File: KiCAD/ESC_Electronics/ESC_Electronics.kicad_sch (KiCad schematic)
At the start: 57 parts, among them J1 -1000VDC, J2 Test Input, J3 CA probe, J4 DC Power, J5 Output, J6 Barrel_Jack, Q1 MMBT3906, Q2 MMBT3904, U1 CR110, U2 SiPhotodiode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

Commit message: laying out V1
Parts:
- added H1, H2, H3, H4: MountingHole, MountingHole:MountingHole_3.2mm_M3, symbol Mechanical:MountingHole
- added J7: -6V, Connector_PinHeader_2.54mm:PinHeader_1x02_P2.54mm_Vertical, symbol Connector_Generic:Conn_01x02
- added J8: +6V, Connector_PinHeader_2.54mm:PinHeader_1x02_P2.54mm_Vertical, symbol Connector_Generic:Conn_01x02
- added TH1: PTC 200mA, Fuse:Fuse_1210_3225Metric_Pad1.42x2.65mm_HandSolder, symbol Device:Thermistor_PTC_US
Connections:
- net +6VDC: now also J8.1 (Pin_1)
- net -6VDC: now also J7.1 (Pin_1)
- net GND: now also J7.2 (Pin_2), J8.2 (Pin_2)
- net at J6.1: now also TH1.2; no longer L1.1
- new net: L1.1, TH1.1
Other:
- moved on the sheet: J6

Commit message: layed out board
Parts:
- added H5: DiodeFeedThru, ESC_Electronics_Library:DiodeFeedThru, symbol Mechanical:MountingHole
- added R20: 10k, Resistor_THT:R_Axial_DIN0207_L6.3mm_D2.5mm_P5.08mm_Vertical, symbol Device:R_Small_US
- C6: value 1nF -> 1pF; Digikey 399-5094-ND -> 445-180733-1-ND
- R11: footprint Resistor_SMD:R_0805_2012Metric_Pad1.20x1.40mm_HandSolder -> Resistor_THT:R_Axial_DIN0207_L6.3mm_D2.5mm_P5.08mm_Vertical
- R12: value 20k -> 10k; footprint Resistor_SMD:R_0805_2012Metric_Pad1.20x1.40mm_HandSolder -> Resistor_THT:R_Axial_DIN0207_L6.3mm_D2.5mm_P5.08mm_Vertical
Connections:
- net GND: now also C9.2, R12.1, U3.4 (VCC-)
- net at J5.1 (In), U3.1 (1OUT): now also R20.2; no longer R12.1
- net at R11.2, U3.3 (1IN+): no longer R12.2
- new net: R12.2, R20.1, U3.2 (1IN-)
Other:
- note added: "A = 1+R20/R12"
- moved on the sheet: J5, R12

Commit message: uploaded this version to OSHpark as V1
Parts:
- added H6, H7: MountingHole, ESC_Electronics_Library:4headclear, symbol Mechanical:MountingHole
- C1, C4: footprint Capacitor_SMD:C_1206_3216Metric_Pad1.33x1.80mm_HandSolder -> Capacitor_SMD:C_0805_2012Metric_Pad1.18x1.45mm_HandSolder; Digikey 1276-6767-1-ND -> 1276-1096-1-ND
- C7: Digikey 445-181037-ND -> 445-175513-ND
- C9: Digikey (none) -> 1276-1099-1-ND
- D1, D2, D3, D4: Digikey (none) -> 3757-RB751V-40-AU_R1_000A1CT-ND
- J6: Digikey 2368-57-PJ70-ND -> 839-1580-ND
- R12: Digikey RNCP0805FTD20K0CT-ND -> (none)
- R18, R19: footprint Resistor_SMD:R_0805_2012Metric_Pad1.20x1.40mm_HandSolder -> Resistor_SMD:R_1206_3216Metric_Pad1.30x1.75mm_HandSolder; Digikey RNCP0805FTD20R0CT-ND -> RNCP1206FTD20R0CT-ND

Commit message: the real ESC V1
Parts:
- U2: footprint Connector_Wire:SolderWire-2sqmm_1x02_P7.8mm_D2mm_OD3.9mm -> Connector_Wire:SolderWire-1sqmm_1x02_P7.8mm_D1.4mm_OD3.9mm
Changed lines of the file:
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@@
     (property "Reference" "U2" (id 0) (at 64.77 66.04 0))
     (property "Value" "SiPhotodiode" (id 1) (at 64.77 80.01 0))
-    (property "Footprint" "Connector_Wire:SolderWire-2sqmm_1x02_P7.8mm_D2mm_OD3.9mm" (id 2) (at 64.77 74.93 0)
+    (property "Footprint" "Connector_Wire:SolderWire-1sqmm_1x02_P7.8mm_D1.4mm_OD3.9mm" (id 2) (at 64.77 74.93 0)
       (effects (font (size 1.27 1.27)) hide)
     )
@@
     )
     (path "/e6c36a61-be9b-4e0e-80a4-d48420033ad2"
-      (reference "U2") (unit 1) (value "SiPhotodiode") (footprint "Connector_Wire:SolderWire-2sqmm_1x02_P7.8mm_D2mm_OD3.9mm")
+      (reference "U2") (unit 1) (value "SiPhotodiode") (footprint "Connector_Wire:SolderWire-1sqmm_1x02_P7.8mm_D1.4mm_OD3.9mm")
     )
     (path "/97bce208-2f33-403f-8d9d-1ed134dba1dc"

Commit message: Refining for V2 while debugging
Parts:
- added C?: 0.1uF, Capacitor_SMD:C_0805_2012Metric_Pad1.18x1.45mm_HandSolder, symbol Device:C_Small
- D5, D6: value MM3Z6V8 -> MM3Z7V5T1G; Digikey MM3Z6V8T1GOSCT-ND -> MM3Z7V5T1GOSCT-ND
- R11, R12, R20: footprint Resistor_THT:R_Axial_DIN0207_L6.3mm_D2.5mm_P5.08mm_Vertical -> Resistor_THT:R_Axial_DIN0207_L6.3mm_D2.5mm_P10.16mm_Horizontal
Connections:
- net -6VDC: now also U3.4 (VCC-), C?.1
- net GND: now also D6.2 (A), C?.2; no longer D6.1 (K), U3.4 (VCC-)
- net at C12.1, Q2.1 (B), R16.2: now also D6.1 (K); no longer D6.2 (A)
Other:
- note added: "V1-V2 Changes: D6 orientation was backwards"
- note added: "V1: Initial Design (works w/ mods) V2: D6 orientation fixed, U3 VCC- power now -6V, change zeener D5/6 to 7.5V"
- moved on the sheet: C9, D6

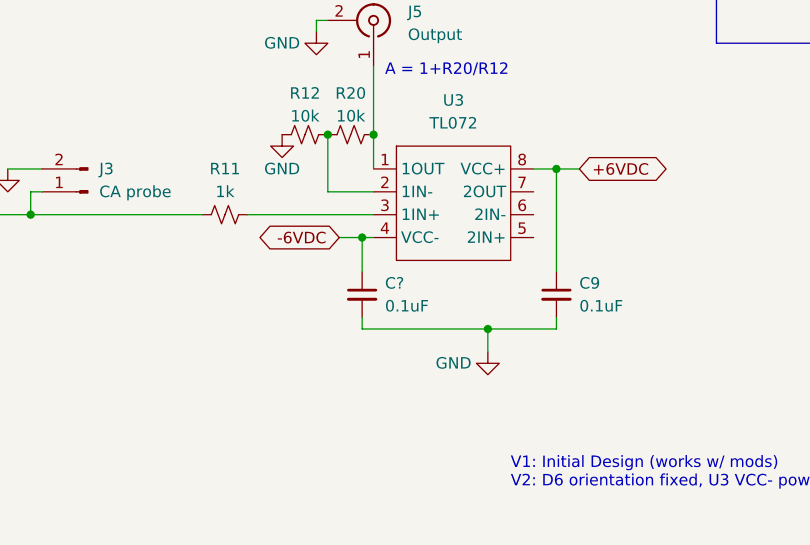
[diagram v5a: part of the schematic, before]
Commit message: Refining for V2 while debugging R2
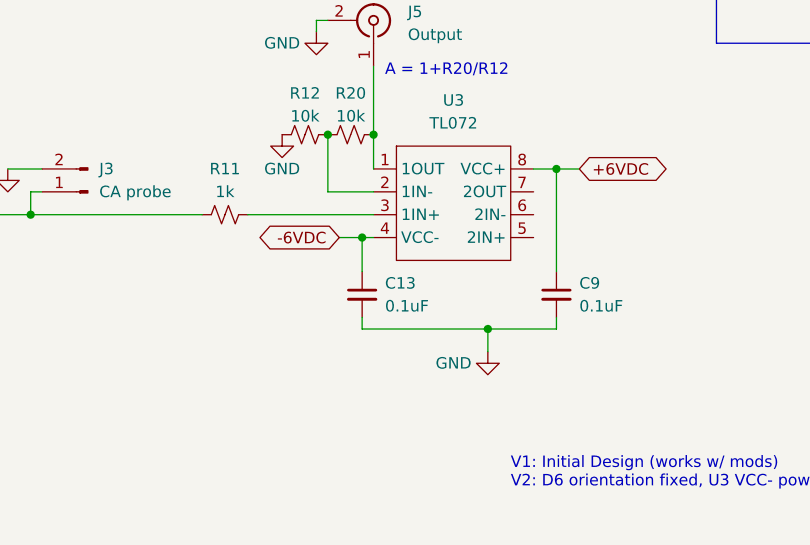
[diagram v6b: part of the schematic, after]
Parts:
- J6: footprint Connector_Wire:SolderWire-0.75sqmm_1x02_P7mm_D1.25mm_OD3.5mm -> Connector_Wire:SolderWire-0.5sqmm_1x02_P4.6mm_D0.9mm_OD2.1mm
- U2: footprint Connector_Wire:SolderWire-1sqmm_1x02_P7.8mm_D1.4mm_OD3.9mm -> Connector_Wire:SolderWire-0.5sqmm_1x02_P4.6mm_D0.9mm_OD2.1mm
- gave numbers to parts that had none: 1
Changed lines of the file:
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@@
   (symbol (lib_id "Device:C_Small") (at 161.29 148.59 0) (unit 1)
     (in_bom yes) (on_board yes) (fields_autoplaced)
-    (property "Reference" "C?" (id 0) (at 163.83 147.3262 0)
+    (property "Reference" "C13" (id 0) (at 163.83 147.3262 0)
       (effects (font (size 1.27 1.27)) (justify left))
     )
@@
     (property "Reference" "J6" (id 0) (at 144.78 59.69 0))
     (property "Value" "Barrel_Jack" (id 1) (at 144.78 62.23 0))
-    (property "Footprint" "Connector_Wire:SolderWire-0.75sqmm_1x02_P7mm_D1.25mm_OD3.5mm" (id 2) (at 146.05 69.596 0)
+    (property "Footprint" "Connector_Wire:SolderWire-0.5sqmm_1x02_P4.6mm_D0.9mm_OD2.1mm" (id 2) (at 146.05 69.596 0)
       (effects (font (size 1.27 1.27)) hide)
     )
@@
     (property "Reference" "U2" (id 0) (at 64.77 66.04 0))
     (property "Value" "SiPhotodiode" (id 1) (at 64.77 80.01 0))
-    (property "Footprint" "Connector_Wire:SolderWire-1sqmm_1x02_P7.8mm_D1.4mm_OD3.9mm" (id 2) (at 64.77 74.93 0)
+    (property "Footprint" "Connector_Wire:SolderWire-0.5sqmm_1x02_P4.6mm_D0.9mm_OD2.1mm" (id 2) (at 64.77 74.93 0)
       (effects (font (size 1.27 1.27)) hide)
     )
@@
     )
     (path "/15f60ce8-f9f6-4219-a4f7-60b75ad13587"
-      (reference "C?") (unit 1) (value "0.1uF") (footprint "Capacitor_SMD:C_0805_2012Metric_Pad1.18x1.45mm_HandSolder")
+      (reference "C13") (unit 1) (value "0.1uF") (footprint "Capacitor_SMD:C_0805_2012Metric_Pad1.18x1.45mm_HandSolder")
     )
     (path "/4279194e-067c-4776-b21d-089a47132a3b"
@@
     )
     (path "/35cfbf87-dcaf-4d5c-832e-d9611d138f98"
-      (reference "J6") (unit 1) (value "Barrel_Jack") (footprint "Connector_Wire:SolderWire-0.75sqmm_1x02_P7mm_D1.25mm_OD3.5mm")
+      (reference "J6") (unit 1) (value "Barrel_Jack") (footprint "Connector_Wire:SolderWire-0.5sqmm_1x02_P4.6mm_D0.9mm_OD2.1mm")
     )
     (path "/9130d071-ea24-455f-bfb6-ea618ccf9d3d"
@@
     )
     (path "/e6c36a61-be9b-4e0e-80a4-d48420033ad2"
-      (reference "U2") (unit 1) (value "SiPhotodiode") (footprint "Connector_Wire:SolderWire-1sqmm_1x02_P7.8mm_D1.4mm_OD3.9mm")
+      (reference "U2") (unit 1) (value "SiPhotodiode") (footprint "Connector_Wire:SolderWire-0.5sqmm_1x02_P4.6mm_D0.9mm_OD2.1mm")
     )
     (path "/97bce208-2f33-403f-8d9d-1ed134dba1dc"

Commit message: Refining for V2 while debugging R3
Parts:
- R3, R4, R5, R6, R8: footprint Resistor_THT:R_Axial_DIN0207_L6.3mm_D2.5mm_P7.62mm_Horizontal -> Resistor_THT:R_Axial_DIN0207_L6.3mm_D2.5mm_P10.16mm_Horizontal
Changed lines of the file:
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@@
       (effects (font (size 1.27 1.27)) (justify right))
     )
-    (property "Footprint" "Resistor_THT:R_Axial_DIN0207_L6.3mm_D2.5mm_P7.62mm_Horizontal" (id 2) (at 77.47 93.98 0)
+    (property "Footprint" "Resistor_THT:R_Axial_DIN0207_L6.3mm_D2.5mm_P10.16mm_Horizontal" (id 2) (at 77.47 93.98 0)
       (effects (font (size 1.27 1.27)) hide)
     )
@@
     (property "Reference" "R5" (id 0) (at 80.01 68.58 90))
     (property "Value" "100M" (id 1) (at 80.01 71.12 90))
-    (property "Footprint" "Resistor_THT:R_Axial_DIN0207_L6.3mm_D2.5mm_P7.62mm_Horizontal" (id 2) (at 80.01 74.93 0)
+    (property "Footprint" "Resistor_THT:R_Axial_DIN0207_L6.3mm_D2.5mm_P10.16mm_Horizontal" (id 2) (at 80.01 74.93 0)
       (effects (font (size 1.27 1.27)) hide)
     )
@@
       (effects (font (size 1.27 1.27)) (justify right))
     )
-    (property "Footprint" "Resistor_THT:R_Axial_DIN0207_L6.3mm_D2.5mm_P7.62mm_Horizontal" (id 2) (at 83.82 101.6 0)
+    (property "Footprint" "Resistor_THT:R_Axial_DIN0207_L6.3mm_D2.5mm_P10.16mm_Horizontal" (id 2) (at 83.82 101.6 0)
       (effects (font (size 1.27 1.27)) hide)
     )
@@
       (effects (font (size 1.27 1.27)) (justify right))
     )
-    (property "Footprint" "Resistor_THT:R_Axial_DIN0207_L6.3mm_D2.5mm_P7.62mm_Horizontal" (id 2) (at 77.47 86.36 0)
+    (property "Footprint" "Resistor_THT:R_Axial_DIN0207_L6.3mm_D2.5mm_P10.16mm_Horizontal" (id 2) (at 77.47 86.36 0)
       (effects (font (size 1.27 1.27)) hide)
     )
@@
     (property "Reference" "R8" (id 0) (at 90.17 68.58 90))
     (property "Value" "10M" (id 1) (at 90.17 71.12 90))
-    (property "Footprint" "Resistor_THT:R_Axial_DIN0207_L6.3mm_D2.5mm_P7.62mm_Horizontal" (id 2) (at 90.17 74.93 0)
+    (property "Footprint" "Resistor_THT:R_Axial_DIN0207_L6.3mm_D2.5mm_P10.16mm_Horizontal" (id 2) (at 90.17 74.93 0)
       (effects (font (size 1.27 1.27)) hide)
     )
@@
     )
     (path "/e9c0533d-0202-41f0-8376-66013cd8499f"
-      (reference "R3") (unit 1) (value "10M") (footprint "Resistor_THT:R_Axial_DIN0207_L6.3mm_D2.5mm_P7.62mm_Horizontal")
+      (reference "R3") (unit 1) (value "10M") (footprint "Resistor_THT:R_Axial_DIN0207_L6.3mm_D2.5mm_P10.16mm_Horizontal")
     )
     (path "/146fe700-c2d8-4e22-bcbd-58e49b24aa20"
-      (reference "R4") (unit 1) (value "10M") (footprint "Resistor_THT:R_Axial_DIN0207_L6.3mm_D2.5mm_P7.62mm_Horizontal")
+      (reference "R4") (unit 1) (value "10M") (footprint "Resistor_THT:R_Axial_DIN0207_L6.3mm_D2.5mm_P10.16mm_Horizontal")
     )
     (path "/5b6ed6c9-23b2-44e2-ac6c-c5f6fd84d8ff"
-      (reference "R5") (unit 1) (value "100M") (footprint "Resistor_THT:R_Axial_DIN0207_L6.3mm_D2.5mm_P7.62mm_Horizontal")
+      (reference "R5") (unit 1) (value "100M") (footprint "Resistor_THT:R_Axial_DIN0207_L6.3mm_D2.5mm_P10.16mm_Horizontal")
     )
     (path "/e23bdf77-1225-4064-a1b7-dcb41f651bc1"
-      (reference "R6") (unit 1) (value "0") (footprint "Resistor_THT:R_Axial_DIN0207_L6.3mm_D2.5mm_P7.62mm_Horizontal")
+      (reference "R6") (unit 1) (value "0") (footprint "Resistor_THT:R_Axial_DIN0207_L6.3mm_D2.5mm_P10.16mm_Horizontal")
     )
     (path "/21ccc60c-91cc-4549-b0cc-a7e03863a2ab"
@@
     )
     (path "/ed44f58b-3ee6-491b-9742-4846733cd8ae"
-      (reference "R8") (unit 1) (value "10M") (footprint "Resistor_THT:R_Axial_DIN0207_L6.3mm_D2.5mm_P7.62mm_Horizontal")
+      (reference "R8") (unit 1) (value "10M") (footprint "Resistor_THT:R_Axial_DIN0207_L6.3mm_D2.5mm_P10.16mm_Horizontal")
     )
     (path "/91550060-841e-4339-a223-2d8cc8600b58"

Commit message: Refining for V2 while debugging R4
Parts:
- added J9: Batt probe, Connector_PinHeader_2.54mm:PinHeader_1x02_P2.54mm_Vertical, symbol Connector:Conn_01x02_Male
- C3, C5: footprint Capacitor_THT:C_Disc_D7.5mm_W5.0mm_P5.00mm -> Capacitor_THT:C_Disc_D10.5mm_W5.0mm_P7.50mm; Digikey 399-5094-ND -> 445-181696-ND
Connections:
- net GND: now also C5.1; no longer C5.2
- net at BT6.1 (+), R4.1: now also J9.1 (Pin_1)
- net at R5.2, R8.1: now also C5.2; no longer C5.1
- net at BT1.2 (-), C7.1, U2.1 (P): now also J9.2 (Pin_2)
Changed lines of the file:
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@@
 (kicad_sch (version 20211123) (generator eeschema)
   (paper "A4")
+  (junction (at 77.47 99.06) (diameter 0) (color 0 0 0 0)
+  )
   (junction (at 83.82 121.92) (diameter 0) (color 0 0 0 0)
   )
@@
   (junction (at 217.17 115.57) (diameter 0) (color 0 0 0 0)
   )
+  (junction (at 52.07 86.36) (diameter 0) (color 0 0 0 0)
+  )
   (junction (at 161.29 142.24) (diameter 0) (color 0 0 0 0)
   )
@@
     (stroke (width 0) (type default) (color 0 0 0 0))
   )
+  (wire (pts (xy 48.26 86.36) (xy 52.07 86.36))
+    (stroke (width 0) (type default) (color 0 0 0 0))
+  )
   (wire (pts (xy 72.39 154.94) (xy 72.39 156.21))
     (stroke (width 0) (type default) (color 0 0 0 0))
@@
     (stroke (width 0) (type default) (color 0 0 0 0))
   )
+  (wire (pts (xy 77.47 107.95) (xy 48.26 107.95))
+    (stroke (width 0) (type default) (color 0 0 0 0))
+  )
   (wire (pts (xy 187.96 81.28) (xy 205.74 81.28))
     (stroke (width 0) (type default) (color 0 0 0 0))
@@
     (stroke (width 0) (type default) (color 0 0 0 0))
   )
+  (wire (pts (xy 48.26 93.98) (xy 48.26 107.95))
+    (stroke (width 0) (type default) (color 0 0 0 0))
+  )
   (wire (pts (xy 69.85 121.92) (xy 62.23 121.92))
     (stroke (width 0) (type default) (color 0 0 0 0))
@@
     (stroke (width 0) (type default) (color 0 0 0 0))
   )
+  (wire (pts (xy 77.47 99.06) (xy 77.47 107.95))
+    (stroke (width 0) (type default) (color 0 0 0 0))
+  )
   (wire (pts (xy 83.82 97.79) (xy 101.6 97.79))
     (stroke (width 0) (type default) (color 0 0 0 0))
@@
   )
   (wire (pts (xy 214.63 46.99) (xy 214.63 49.53))
+    (stroke (width 0) (type default) (color 0 0 0 0))
+  )
+  (wire (pts (xy 48.26 86.36) (xy 48.26 91.44))
     (stroke (width 0) (type default) (color 0 0 0 0))
   )
@@
     (pin "2")
   )
+  (symbol (lib_id "Device:C_Small") (at 104.14 85.09 270) (unit 1)
+    (in_bom yes) (on_board yes) (fields_autoplaced)
+    (property "Reference" "C5" (id 0) (at 104.1336 79.8281 90))
+    (property "Value" "1nF" (id 1) (at 104.1336 82.365 90))
+    (property "Footprint" "Capacitor_THT:C_Disc_D10.5mm_W5.0mm_P7.50mm" (id 2) (at 104.14 85.09 0)
+      (effects (font (size 1.27 1.27)) hide)
+    )
+    (property "Datasheet" "https://www.digikey.com/en/products/detail/tdk-corporation/CK45-B3FD102KYGNA/4457522" (id 3) (at 104.14 85.09 0)
+      (effects (font (size 1.27 1.27)) hide)
+    )
+    (property "Digikey" "445-181696-ND" (id 4) (at 104.14 85.09 90)
+      (effects (font (size 1.27 1.27)) hide)
+    )
+    (pin "1")
+    (pin "2")
+  )
   (symbol (lib_id "power:GND") (at 68.58 124.46 0) (unit 1)
     (in_bom yes) (on_board yes) (fields_autoplaced)
@@
     (pin "2")
   )
-  (symbol (lib_id "Device:C_Small") (at 104.14 85.09 90) (unit 1)
-    (in_bom yes) (on_board yes)
-    (property "Reference" "C5" (id 0) (at 101.6 80.01 90))
-    (property "Value" "1nF" (id 1) (at 101.6 82.55 90))
-    (property "Footprint" "Capacitor_THT:C_Disc_D7.5mm_W5.0mm_P5.00mm" (id 2) (at 104.14 85.09 0)
-      (effects (font (size 1.27 1.27)) hide)
-    )
-    (property "Datasheet" "https://www.digikey.com/en/products/detail/kemet/C330C102JHR5TA/1465599" (id 3) (at 104.14 85.09 0)
-      (effects (font (size 1.27 1.27)) hide)
-    )
-    (property "Digikey" "399-5094-ND" (id 4) (at 104.14 85.09 90)
-      (effects (font (size 1.27 1.27)) hide)
-    )
-    (pin "1")
-    (pin "2")
-  )
   (symbol (lib_id "Connector:Conn_Coaxial") (at 105.41 121.92 0) (unit 1)
     (in_bom yes) (on_board yes) (fields_autoplaced)
@@
     )
     (property "Digikey" "RNCP1206FTD20R0CT-ND" (id 4) (at 222.25 34.29 0)
+      (effects (font (size 1.27 1.27)) hide)
+    )
+    (pin "1")
+    (pin "2")
+  )
+  (symbol (lib_id "Connector:Conn_01x02_Male") (at 43.18 93.98 0) (mirror x) (unit 1)
+    (in_bom yes) (on_board yes) (fields_autoplaced)
+    (property "Reference" "J9" (id 0) (at 42.4688 91.8753 0)
+      (effects (font (size 1.27 1.27)) (justify right))
+    )
+    (property "Value" "Batt probe" (id 1) (at 42.4688 94.4122 0)
+      (effects (font (size 1.27 1.27)) (justify right))
+    )
+    (property "Footprint" "Connector_PinHeader_2.54mm:PinHeader_1x02_P2.54mm_Vertical" (id 2) (at 43.18 93.98 0)
+      (effects (font (size 1.27 1.27)) hide)
+    )
+    (property "Datasheet" "~" (id 3) (at 43.18 93.98 0)
       (effects (font (size 1.27 1.27)) hide)
     )
@@
       (effects (font (size 1.27 1.27)) (justify right))
     )
-    (property "Footprint" "Capacitor_THT:C_Disc_D7.5mm_W5.0mm_P5.00mm" (id 2) (at 83.82 109.22 0)
-      (effects (font (size 1.27 1.27)) hide)
-    )
-    (property "Datasheet" "https://www.digikey.com/en/products/detail/kemet/C330C102JHR5TA/1465599" (id 3) (at 83.82 109.22 0)
-      (effects (font (size 1.27 1.27)) hide)
-    )
-    (property "Digikey" "399-5094-ND" (id 4) (at 83.82 109.22 90)
+    (property "Footprint" "Capacitor_THT:C_Disc_D10.5mm_W5.0mm_P7.50mm" (id 2) (at 83.82 109.22 0)
+      (effects (font (size 1.27 1.27)) hide)
+    )
+    (property "Datasheet" "https://www.digikey.com/en/products/detail/tdk-corporation/CK45-B3FD102KYGNA/4457522" (id 3) (at 83.82 109.22 0)
+      (effects (font (size 1.27 1.27)) hide)
+    )
+    (property "Digikey" "445-181696-ND" (id 4) (at 83.82 109.22 90)
       (effects (font (size 1.27 1.27)) hide)
     )
@@
     )
     (path "/c43b88c4-8909-4dde-a63c-d6374c47ed09"
-      (reference "C3") (unit 1) (value "1nF") (footprint "Capacitor_THT:C_Disc_D7.5mm_W5.0mm_P5.00mm")
+      (reference "C3") (unit 1) (value "1nF") (footprint "Capacitor_THT:C_Disc_D10.5mm_W5.0mm_P7.50mm")
     )
     (path "/75bdc966-fa8f-4b3c-aaff-f2527f373b5c"
       (reference "C4") (unit 1) (value "10uF") (footprint "Capacitor_SMD:C_0805_2012Metric_Pad1.18x1.45mm_HandSolder")
     )
-    (path "/0e713fdd-cb6b-45cd-920b-65c543e12350"
-      (reference "C5") (unit 1) (value "1nF") (footprint "Capacitor_THT:C_Disc_D7.5mm_W5.0mm_P5.00mm")
+    (path "/036241d1-8d8d-45ff-b94f-b678de147046"
+      (reference "C5") (unit 1) (value "1nF") (footprint "Capacitor_THT:C_Disc_D10.5mm_W5.0mm_P7.50mm")
     )
     (path "/d0973795-48d6-4222-9434-7472eaf00111"
@@
       (reference "J8") (unit 1) (value "+6V") (footprint "Connector_PinHeader_2.54mm:PinHeader_1x02_P2.54mm_Vertical")
     )
+    (path "/36c9aedf-6b7b-47ea-98a1-5bc4e2310db1"
+      (reference "J9") (unit 1) (value "Batt probe") (footprint "Connector_PinHeader_2.54mm:PinHeader_1x02_P2.54mm_Vertical")
+    )
     (path "/6d7863b7-f00b-4dbe-87ea-68fac5c86730"
